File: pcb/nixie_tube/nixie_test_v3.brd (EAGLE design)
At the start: 50.2 x 23.5 mm, 10 parts, among them IC1 74141N

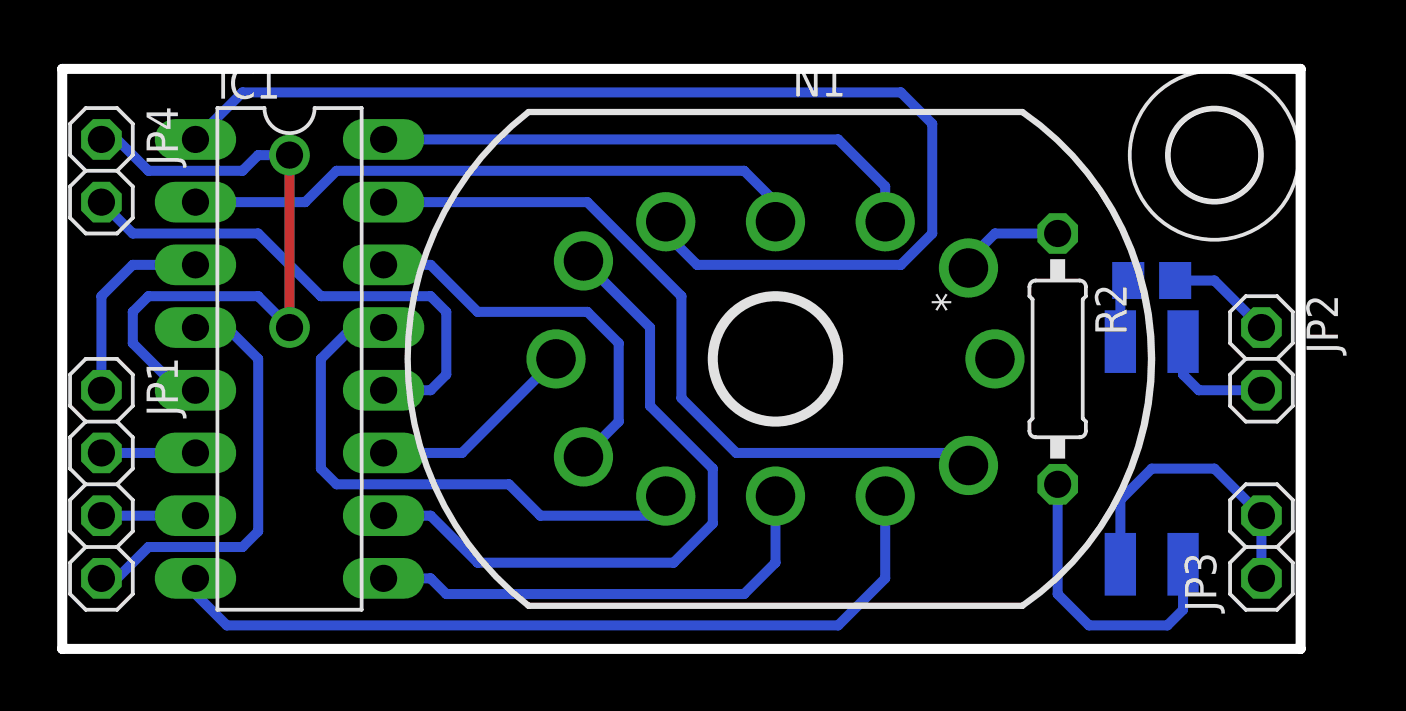
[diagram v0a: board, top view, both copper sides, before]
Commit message: 
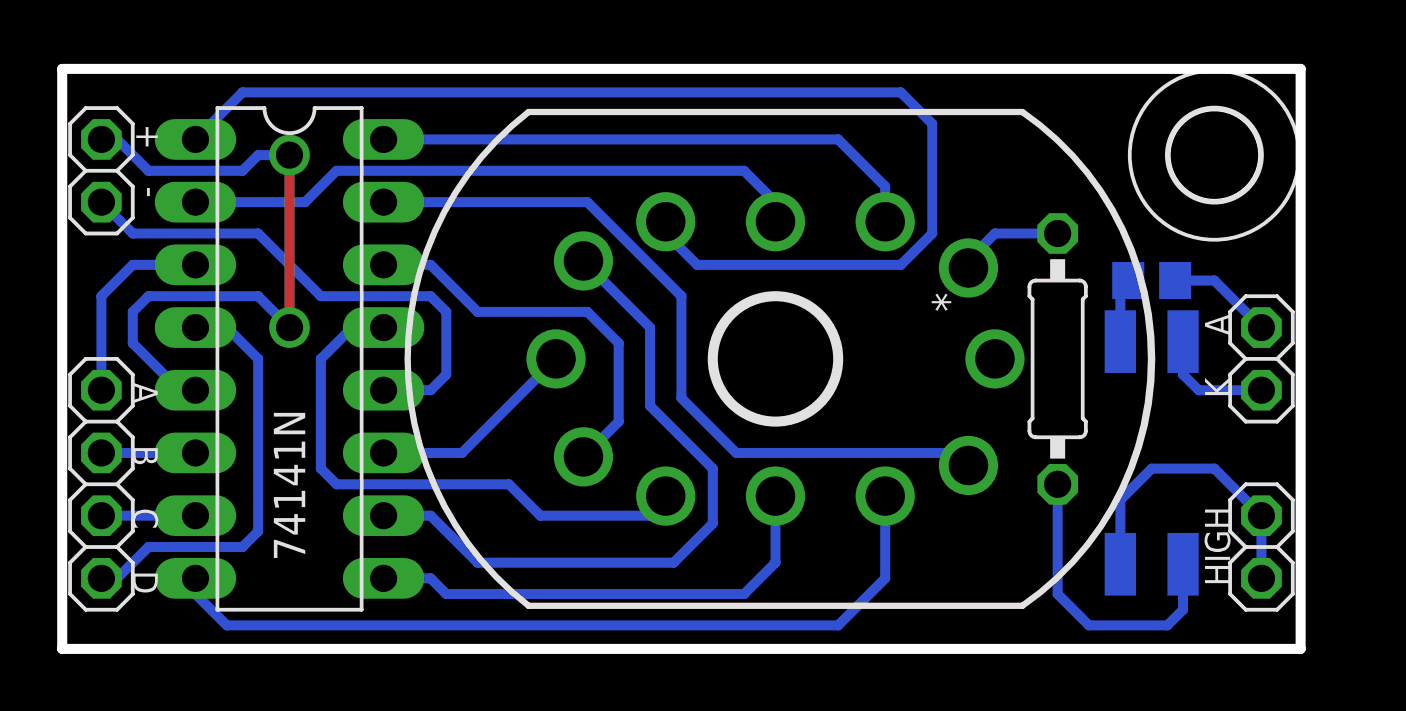
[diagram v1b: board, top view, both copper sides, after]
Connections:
- net +24V renamed +180V
- net N$2 renamed LK
- net N$6 renamed LA
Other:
- board text added: "+"
- board text added: "-"
- board text added: "A"
- board text added: "B"
- board text added: "C"
- board text added: "D"
- board text added: "HIGH"
- board text added: "K"
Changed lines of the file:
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@@
 <layer number="35" name="tGlue" color="7" fill="4" visible="no" active="yes"/>
 <layer number="36" name="bGlue" color="7" fill="5" visible="no" active="yes"/>
-<layer number="37" name="tTest" color="7" fill="1" visible="yes" active="yes"/>
-<layer number="38" name="bTest" color="7" fill="1" visible="yes" active="yes"/>
+<layer number="37" name="tTest" color="7" fill="1" visible="no" active="yes"/>
+<layer number="38" name="bTest" color="7" fill="1" visible="no" active="yes"/>
 <layer number="39" name="tKeepout" color="4" fill="11" visible="no" active="yes"/>
 <layer number="40" name="bKeepout" color="1" fill="11" visible="no" active="yes"/>
@@
 <layer number="46" name="Milling" color="3" fill="1" visible="no" active="yes"/>
 <layer number="47" name="Measures" color="7" fill="1" visible="no" active="yes"/>
-<layer number="48" name="Document" color="7" fill="1" visible="yes" active="yes"/>
-<layer number="49" name="Reference" color="7" fill="1" visible="yes" active="yes"/>
+<layer number="48" name="Document" color="7" fill="1" visible="no" active="yes"/>
+<layer number="49" name="Reference" color="7" fill="1" visible="no" active="yes"/>
 <layer number="50" name="dxf" color="7" fill="1" visible="no" active="no"/>
 <layer number="51" name="tDocu" color="7" fill="1" visible="yes" active="yes"/>
@@
 <wire x1="50.4825" y1="0.3175" x2="50.4825" y2="23.8125" width="0.4064" layer="20"/>
 <wire x1="50.4825" y1="23.8125" x2="0.3175" y2="23.8125" width="0.4064" layer="20"/>
+<text x="3.175" y="21.59" size="1.016" layer="25" font="vector" ratio="10" rot="R270">+</text>
+<text x="3.175" y="19.05" size="1.016" layer="25" font="vector" ratio="10" rot="R270">-</text>
+<text x="3.175" y="11.1125" size="1.016" layer="25" font="vector" ratio="10" rot="SR270">A</text>
+<text x="3.175" y="8.5725" size="1.016" layer="25" font="vector" ratio="10" rot="SR270">B</text>
+<text x="3.175" y="6.0325" size="1.016" layer="25" font="vector" ratio="10" rot="SR270">C</text>
+<text x="3.175" y="3.4925" size="1.016" layer="25" font="vector" ratio="10" rot="SR270">D</text>
+<text x="47.625" y="13.0175" size="1.016" layer="25" font="vector" ratio="10" rot="R90">A</text>
+<text x="47.625" y="10.4775" size="1.016" layer="25" font="vector" ratio="10" rot="R90">K</text>
+<text x="47.625" y="2.8575" size="1.016" layer="25" font="vector" ratio="10" rot="R90">HIGH</text>
 </plain>
 <attributes>
@@
 </autorouter>
 <elements>
-<element name="N1" library="nixie_tube" package="IN-12" value="IN-12B" x="29.21" y="12.065" rot="R90"/>
-<element name="R2" library="nixie_tube" package="0207/10" value="" x="40.64" y="12.065" rot="R270"/>
-<element name="OK1" library="nixie_tube" package="4-SMD" value="TLP627" x="44.45" y="8.255" rot="MR270">
+<element name="N1" library="nixie_tube" package="IN-12" value="IN-12B" x="29.21" y="12.065" smashed="yes" rot="R90"/>
+<element name="R2" library="nixie_tube" package="0207/10" value="" x="40.64" y="12.065" smashed="yes" rot="R270">
+<attribute name="VALUE" x="40.005" y="14.3256" size="1.27" layer="27" ratio="10" rot="R270"/>
+</element>
+<element name="OK1" library="nixie_tube" package="4-SMD" value="TLP627" x="44.45" y="8.255" smashed="yes" rot="MR270">
 <attribute name="OC_NEWARK" value="unknown" x="81.28" y="-10.795" size="1.778" layer="28" rot="MR270" display="off"/>
 <attribute name="MPN" value="" x="81.28" y="-10.795" size="1.778" layer="28" rot="MR270" display="off"/>
 <attribute name="MF" value="" x="81.28" y="-10.795" size="1.778" layer="28" rot="MR270" display="off"/>
 <attribute name="OC_FARNELL" value="unknown" x="81.28" y="-10.795" size="1.778" layer="28" rot="MR270" display="off"/>
-</element>
-<element name="R1" library="nixie_tube" package="R0805" value="" x="44.45" y="15.24" rot="MR0"/>
-<element name="JP2" library="nixie_tube" package="1X02" value="" x="48.895" y="12.065" rot="R270"/>
-<element name="JP3" library="nixie_tube" package="1X02" value="" x="48.895" y="4.445" rot="R90"/>
-<element name="U$1" library="nixie_tube" package="3,6" value="" x="46.99" y="20.32" rot="R270"/>
-<element name="IC1" library="nixie_tube" package="DIL16" value="74141N" x="9.525" y="12.065" rot="R270"/>
-<element name="JP1" library="nixie_tube" package="1X04" value="" x="1.905" y="6.985" rot="R270"/>
-<element name="JP4" library="nixie_tube" package="1X02" value="" x="1.905" y="19.685" rot="R270"/>
+<attribute name="NAME" x="45.085" y="9.8425" size="1.27" layer="26" rot="MR270"/>
+<attribute name="VALUE" x="47.625" y="11.43" size="1.27" layer="26" rot="MR270"/>
+</element>
+<element name="R1" library="nixie_tube" package="R0805" value="" x="44.45" y="15.24" smashed="yes" rot="MR0">
+<attribute name="VALUE" x="45.085" y="12.7" size="1.27" layer="28" rot="MR0"/>
+</element>
+<element name="JP2" library="nixie_tube" package="1X02" value="" x="48.895" y="12.065" smashed="yes" rot="R270">
+<attribute name="VALUE" x="45.72" y="14.605" size="1.27" layer="27" rot="R270"/>
+</element>
+<element name="JP3" library="nixie_tube" package="1X02" value="" x="48.895" y="4.445" smashed="yes" rot="R90">
+<attribute name="VALUE" x="52.07" y="1.905" size="1.27" layer="27" rot="R90"/>
+</element>
+<element name="U$1" library="nixie_tube" package="3,6" value="" x="46.99" y="20.32" smashed="yes" rot="R270"/>
+<element name="IC1" library="nixie_tube" package="DIL16" value="74141N" x="9.525" y="12.065" smashed="yes" rot="R270">
+<attribute name="VALUE" x="8.89" y="10.033" size="1.27" layer="25" ratio="10" rot="R270"/>
+</element>
+<element name="JP1" library="nixie_tube" package="1X04" value="" x="1.905" y="6.985" smashed="yes" rot="R270">
+<attribute name="VALUE" x="-1.27" y="12.065" size="1.27" layer="27" rot="R270"/>
+</element>
+<element name="JP4" library="nixie_tube" package="1X02" value="" x="1.905" y="19.685" smashed="yes" rot="R270">
+<attribute name="VALUE" x="-1.27" y="22.225" size="1.27" layer="27" rot="R270"/>
+</element>
 </elements>
 <signals>
@@
 <wire x1="45.72" y1="3.175" x2="45.72" y2="3.745" width="0" layer="19" extent="16-16"/>
 </signal>
-<signal name="+24V">
+<signal name="+180V">
 <contactref element="OK1" pad="4"/>
 <contactref element="JP3" pad="1"/>
@@
 <wire x1="43.18" y1="14.92" x2="43.5" y2="15.24" width="0.4064" layer="16"/>
 </signal>
-<signal name="N$2">
+<signal name="LK">
 <contactref element="JP2" pad="2"/>
 <contactref element="OK1" pad="2"/>
@@
 <wire x1="3.175" y1="17.145" x2="1.905" y2="18.415" width="0.4064" layer="16"/>
 </signal>
-<signal name="N$6">
+<signal name="LA">
 <contactref element="JP2" pad="1"/>
 <contactref element="R1" pad="1"/>

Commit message: 
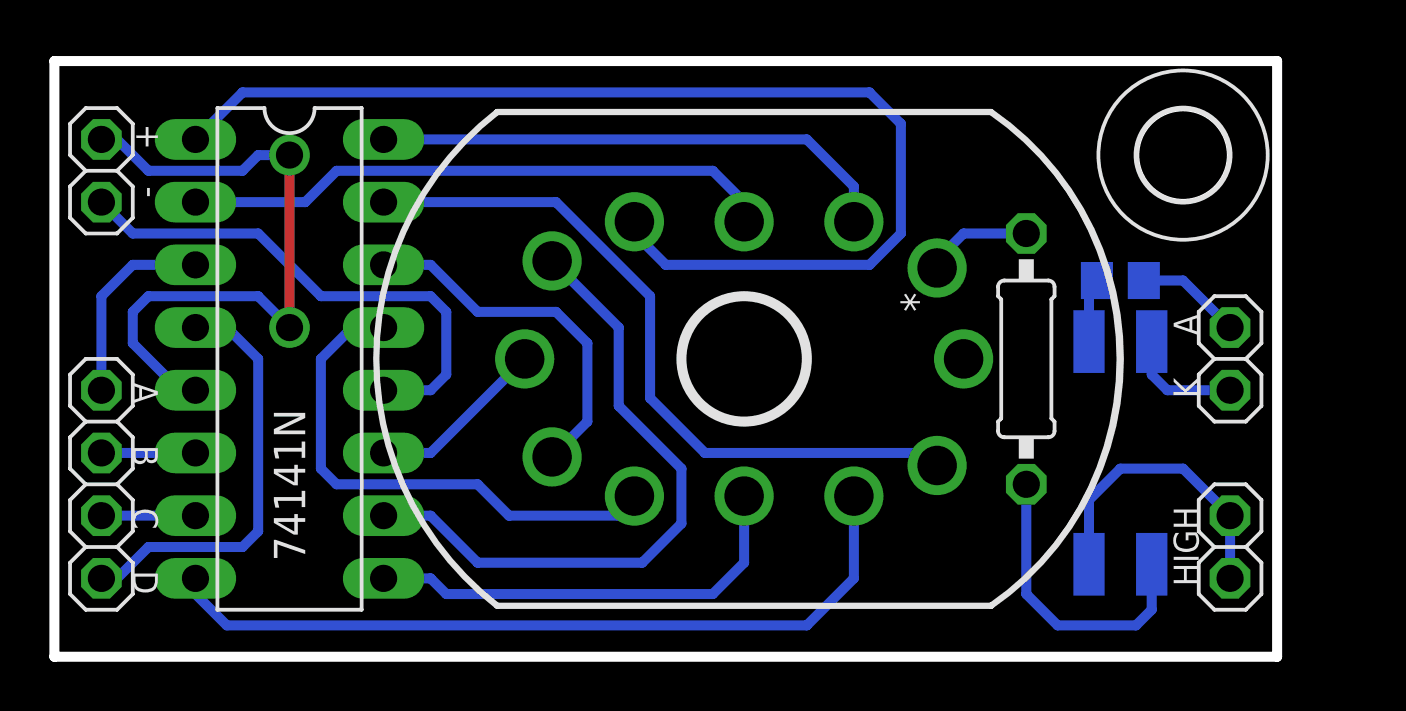
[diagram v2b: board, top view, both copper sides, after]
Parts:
- moved JP2 1.27 mm to (47.6, 12.1)
- moved JP3 1.27 mm to (47.6, 4.45)
- moved OK1 1.27 mm to (43.2, 8.26)
- moved R1 1.27 mm to (43.2, 15.2)
- moved R2 1.27 mm to (39.4, 12.1)
- moved U$1 1.27 mm to (45.7, 20.3)
- moved N1 1.27 mm to (27.9, 12.1)
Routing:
- net C8: track 47.9 -> 46.7 mm
- net C7: track 27.6 -> 26.3 mm
- net C4: track 22.7 -> 21.4 mm
- net C2: track 33.2 -> 32.0 mm
- net C1: track 30.7 -> 29.4 mm
- net C0: track 22.5 -> 21.3 mm
- net C9: track 25.3 -> 24.1 mm
- net C6: track 8.56 -> 7.29 mm
- net C3: track 19.4 -> 18.1 mm
- net C5: track 16.0 -> 14.8 mm
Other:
- board size 50.2 x 23.5 mm -> 49.5 x 24.1 mm

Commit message: 
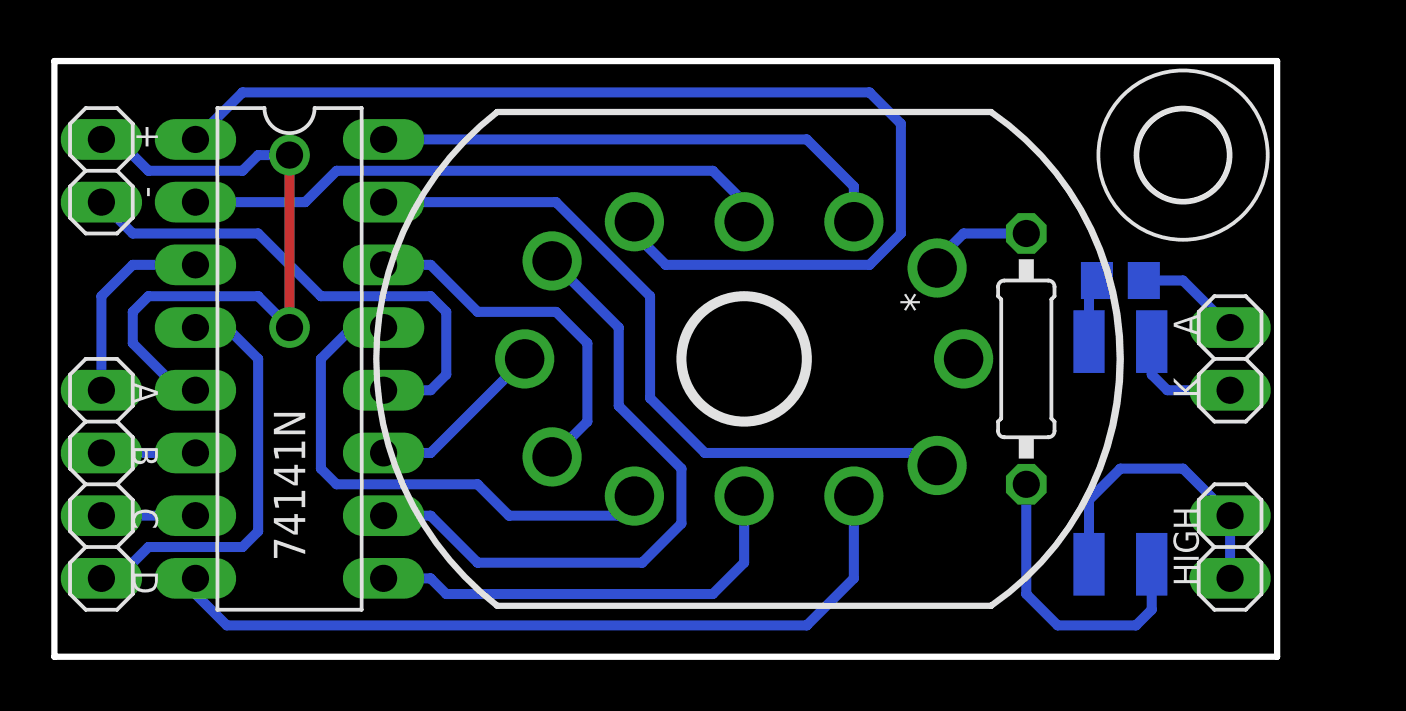
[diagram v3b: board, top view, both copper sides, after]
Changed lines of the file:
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@@
 <layer number="109" name="fp9" color="7" fill="1" visible="no" active="yes"/>
 <layer number="110" name="fp0" color="7" fill="1" visible="no" active="yes"/>
+<layer number="111" name="LPC17xx" color="7" fill="1" visible="yes" active="yes"/>
+<layer number="112" name="tSilk" color="7" fill="1" visible="yes" active="yes"/>
+<layer number="116" name="Patch_BOT" color="9" fill="4" visible="yes" active="yes"/>
 <layer number="121" name="_tsilk" color="7" fill="1" visible="no" active="yes"/>
 <layer number="122" name="_bsilk" color="7" fill="1" visible="no" active="yes"/>
@@
 <layer number="124" name="bTestmark" color="7" fill="1" visible="no" active="yes"/>
 <layer number="125" name="_tNames" color="7" fill="1" visible="no" active="yes"/>
+<layer number="126" name="_bNames" color="7" fill="1" visible="yes" active="yes"/>
+<layer number="127" name="_tValues" color="7" fill="1" visible="yes" active="yes"/>
+<layer number="128" name="_bValues" color="7" fill="1" visible="yes" active="yes"/>
 <layer number="131" name="tAdjust" color="7" fill="1" visible="no" active="yes"/>
 <layer number="132" name="bAdjust" color="7" fill="1" visible="no" active="yes"/>
 <layer number="144" name="Drill_legend" color="7" fill="1" visible="no" active="yes"/>
 <layer number="151" name="HeatSink" color="7" fill="1" visible="no" active="yes"/>
+<layer number="152" name="_bDocu" color="7" fill="1" visible="yes" active="yes"/>
 <layer number="199" name="Contour" color="7" fill="1" visible="no" active="yes"/>
 <layer number="200" name="200bmp" color="1" fill="10" visible="no" active="no"/>
@@
 <layer number="220" name="220bmp" color="21" fill="1" visible="no" active="no"/>
 <layer number="221" name="221bmp" color="22" fill="1" visible="no" active="no"/>
+<layer number="222" name="222bmp" color="23" fill="1" visible="no" active="no"/>
 <layer number="223" name="223bmp" color="24" fill="1" visible="no" active="no"/>
 <layer number="224" name="224bmp" color="25" fill="1" visible="no" active="no"/>
+<layer number="248" name="Housing" color="7" fill="1" visible="yes" active="yes"/>
+<layer number="249" name="Edge" color="7" fill="1" visible="yes" active="yes"/>
 <layer number="250" name="Descript" color="3" fill="1" visible="no" active="no"/>
 <layer number="251" name="SMDround" color="12" fill="11" visible="no" active="no"/>
@@
 <text x="46.355" y="10.4775" size="1.016" layer="25" font="vector" ratio="10" rot="R90">K</text>
 <text x="46.355" y="2.8575" size="1.016" layer="25" font="vector" ratio="10" rot="R90">HIGH</text>
-<wire x1="0" y1="0" x2="0" y2="24.13" width="0.4064" layer="20"/>
-<wire x1="0" y1="24.13" x2="49.53" y2="24.13" width="0.4064" layer="20"/>
-<wire x1="49.53" y1="24.13" x2="49.53" y2="0" width="0.4064" layer="20"/>
-<wire x1="49.53" y1="0" x2="0" y2="0" width="0.4064" layer="20"/>
+<wire x1="0" y1="0" x2="0" y2="24.13" width="0.254" layer="20"/>
+<wire x1="0" y1="24.13" x2="49.53" y2="24.13" width="0.254" layer="20"/>
+<wire x1="49.53" y1="24.13" x2="49.53" y2="0" width="0.254" layer="20"/>
+<wire x1="49.53" y1="0" x2="0" y2="0" width="0.254" layer="20"/>
 </plain>
 <attributes>
